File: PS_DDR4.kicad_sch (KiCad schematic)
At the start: 2 parts, among them U12 K4A8G165WC-BCTD

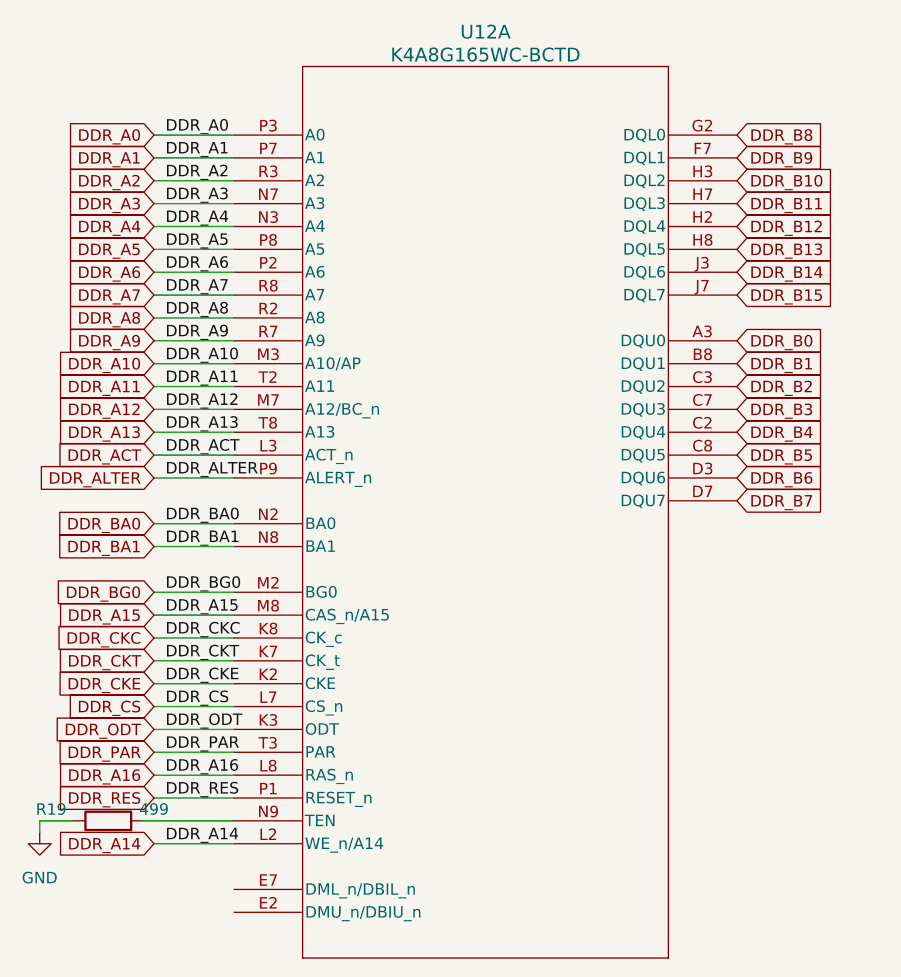
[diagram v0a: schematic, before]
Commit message: DDR4 added
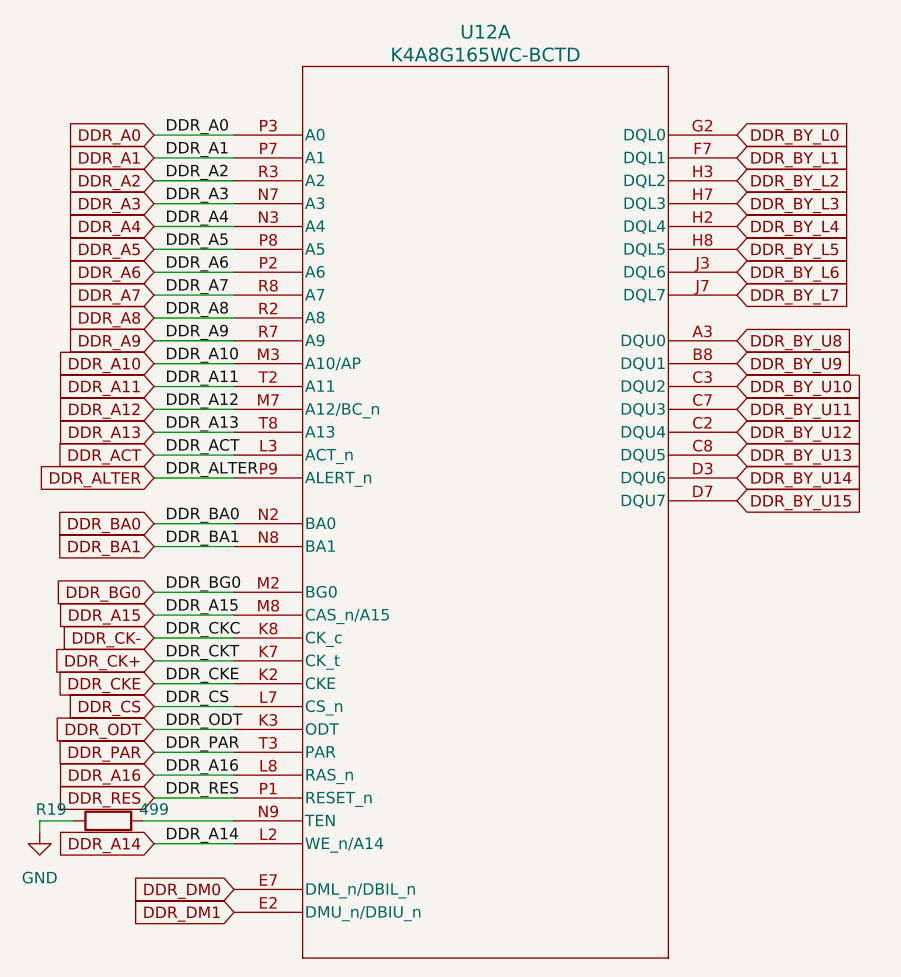
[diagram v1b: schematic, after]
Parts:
- R19: footprint (none) -> Resistor_SMD:R_0402_1005Metric_Pad0.72x0.64mm_HandSolder
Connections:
- net DDR_DM1: now reaches U12.E2 (DMU_n/DBIU_n)
- net DDR_DM0: now reaches U12.E7 (DML_n/DBIL_n)
- net DDR_B0 renamed DDR_BY_U8
- net DDR_B1 renamed DDR_BY_U9
- net DDR_B10 renamed DDR_BY_L2
- net DDR_B11 renamed DDR_BY_L3
- net DDR_B12 renamed DDR_BY_L4
- net DDR_B13 renamed DDR_BY_L5
- net DDR_B14 renamed DDR_BY_L6
- net DDR_B15 renamed DDR_BY_L7
- net DDR_B2 renamed DDR_BY_U10
- net DDR_B3 renamed DDR_BY_U11
- net DDR_B4 renamed DDR_BY_U12
- net DDR_B5 renamed DDR_BY_U13
- net DDR_B6 renamed DDR_BY_U14
- net DDR_B7 renamed DDR_BY_U15
- net DDR_B8 renamed DDR_BY_L0
- net DDR_B9 renamed DDR_BY_L1
- net DDR_CKC renamed DDR_CK-
- net DDR_CKT renamed DDR_CK+

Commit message: Stuff
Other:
- moved on the sheet: R19, U12A

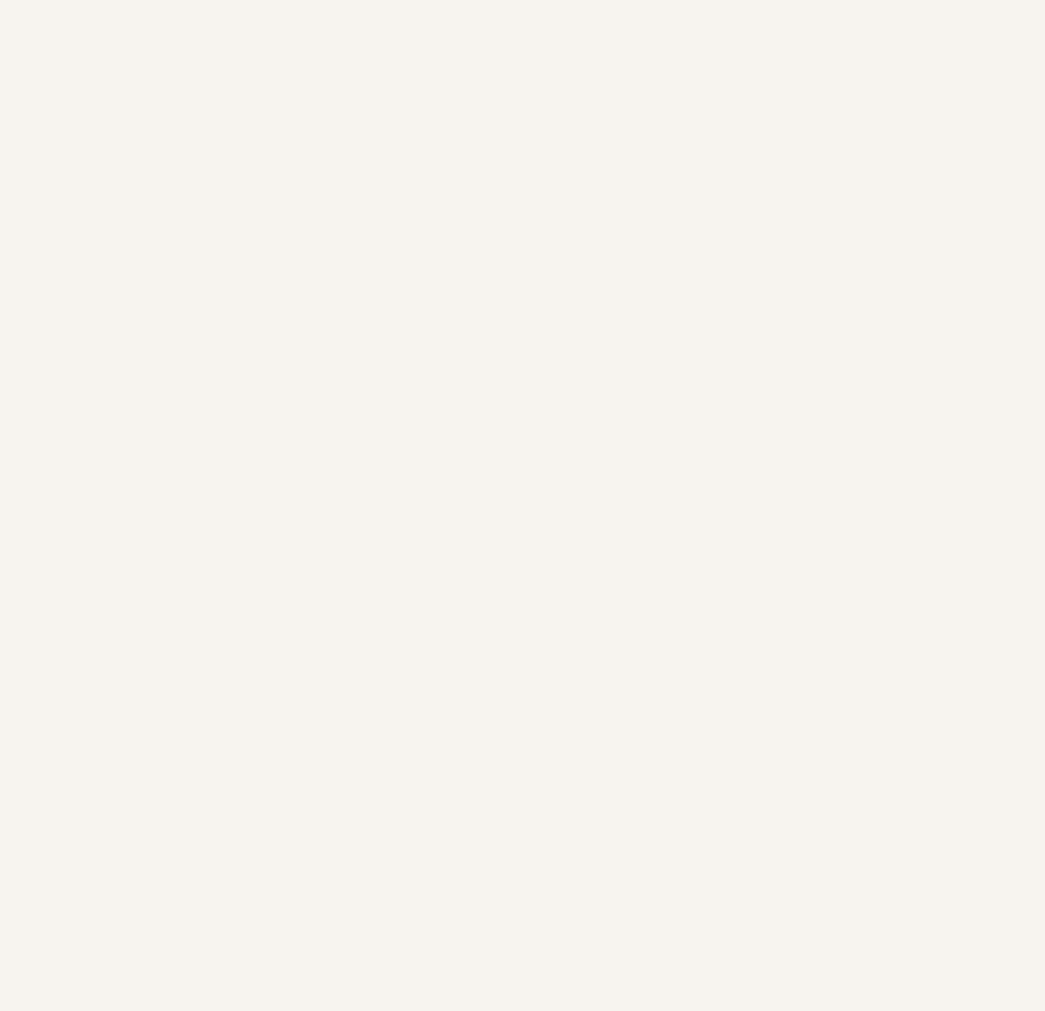
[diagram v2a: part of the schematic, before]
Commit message: DDR4 data lines
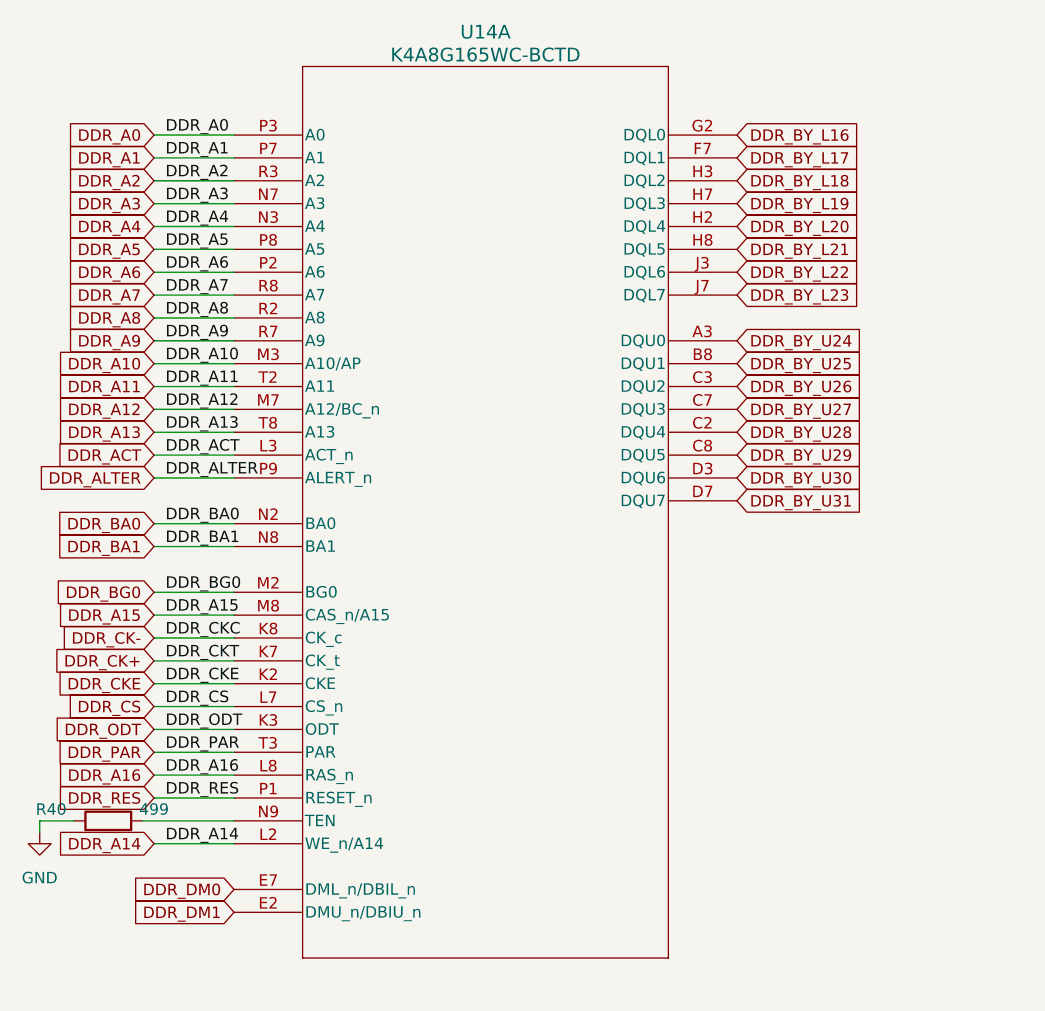
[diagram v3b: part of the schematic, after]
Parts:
- added R40: 499, Resistor_SMD:R_0402_1005Metric_Pad0.72x0.64mm_HandSolder, symbol Device:R
- added U14: K4A8G165WC-BCTD, lib:FBGA96X16_7P5X13P3_SAM, symbol K4A8G165W:K4A8G165WC-BCTD
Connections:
- net DDR_A0: now also U14.P3 (A0)
- net DDR_A1: now also U14.P7 (A1)
- net DDR_A10: now also U14.M3 (A10/AP)
- net DDR_A11: now also U14.T2 (A11)
- net DDR_A12: now also U14.M7 (A12/BC_n)
- net DDR_A13: now also U14.T8 (A13)
- net DDR_A14: now also U14.L2 (WE_n/A14)
- net DDR_A15: now also U14.M8 (CAS_n/A15)
- net DDR_A16: now also U14.L8 (RAS_n)
- net DDR_A2: now also U14.R3 (A2)
- net DDR_A3: now also U14.N7 (A3)
- net DDR_A4: now also U14.N3 (A4)
- net DDR_A5: now also U14.P8 (A5)
- net DDR_A6: now also U14.P2 (A6)
- net DDR_A7: now also U14.R8 (A7)
- net DDR_A8: now also U14.R2 (A8)
- net DDR_A9: now also U14.R7 (A9)
- net DDR_ACT: now also U14.L3 (ACT_n)
- net DDR_ALTER: now also U14.P9 (ALERT_n)
- net DDR_BA0: now also U14.N2 (BA0)
- net DDR_BA1: now also U14.N8 (BA1)
- net DDR_BG0: now also U14.M2 (BG0)
- net DDR_CK+: now also U14.K7 (CK_t)
- net DDR_CK-: now also U14.K8 (CK_c)
- net DDR_CKE: now also U14.K2 (CKE)
- net DDR_CS: now also U14.L7 (CS_n)
- net DDR_DM0: now also U14.E7 (DML_n/DBIL_n)
- net DDR_DM1: now also U14.E2 (DMU_n/DBIU_n)
- net DDR_ODT: now also U14.K3 (ODT)
- net DDR_PAR: now also U14.T3 (PAR)
- net DDR_RES: now also U14.P1 (RESET_n)
- net GND: now also R40.1
- new net: R40.2, U14.N9 (TEN)
- new net DDR_BY_L16: U14.G2 (DQL0)
- new net DDR_BY_L17: U14.F7 (DQL1)
- new net DDR_BY_L18: U14.H3 (DQL2)
- new net DDR_BY_L19: U14.H7 (DQL3)
- new net DDR_BY_L20: U14.H2 (DQL4)
- new net DDR_BY_L21: U14.H8 (DQL5)
- new net DDR_BY_L22: U14.J3 (DQL6)
- new net DDR_BY_L23: U14.J7 (DQL7)
- new net DDR_BY_U24: U14.A3 (DQU0)
- new net DDR_BY_U25: U14.B8 (DQU1)
- new net DDR_BY_U26: U14.C3 (DQU2)
- new net DDR_BY_U27: U14.C7 (DQU3)
- new net DDR_BY_U28: U14.C2 (DQU4)
- new net DDR_BY_U29: U14.C8 (DQU5)
- new net DDR_BY_U30: U14.D3 (DQU6)
- new net DDR_BY_U31: U14.D7 (DQU7)

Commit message: DDR4 finish
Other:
- moved on the sheet: R19, R40, U12A, U14A
